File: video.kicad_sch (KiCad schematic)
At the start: 32 parts

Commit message: だいたい完成
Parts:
- removed U? (x2): 74LS195, symbol 74xx:74LS195
- removed U?: SST39SF010A, symbol RAM_ROM:SST39SF010A
- removed U?: TC551001, symbol RAM_ROM:TC551001
- added U10: TC551001, Package_DIP:DIP-32_W15.24mm, symbol RAM_ROM:TC551001
- added U11: SST39SF010A, Package_DIP:DIP-32_W15.24mm, symbol RAM_ROM:SST39SF010A
- added U8, U9: 74LS195, Package_DIP:DIP-16_W7.62mm, symbol 74xx:74LS195
- C17, C18: renamed from C?; footprint (none) -> Capacitor_THT:C_Disc_D3.0mm_W1.6mm_P2.50mm
- J1: renamed from J?; footprint (none) -> Connector_Dsub:DSUB-15-HD_Female_Horizontal_P2.29x1.98mm_EdgePinOffset3.03mm_Housed_MountingHolesOffset4.94mm
- JP1: renamed from JP?; footprint (none) -> Jumper:SolderJumper-3_P1.3mm_Bridged12_Pad1.0x1.5mm
- R1: renamed from R?; footprint (none) -> Resistor_THT:R_Axial_DIN0204_L3.6mm_D1.6mm_P5.08mm_Vertical
- R2, R3, R4, R5, R6, R7: renamed from R?; footprint (none) -> Resistor_SMD:R_0603_1608Metric_Pad0.98x0.95mm_HandSolder
- SW1: renamed from SW?; footprint (none) -> Button_Switch_THT:SW_DIP_SPSTx03_Slide_9.78x9.8mm_W7.62mm_P2.54mm
- U1, U2, U3: renamed from U?; footprint (none) -> Package_DIP:DIP-14_W7.62mm
- U4, U7: renamed from U?; footprint (none) -> Package_DIP:DIP-16_W7.62mm
- U5: renamed from U?; footprint (none) -> Package_DIP:DIP-20_W7.62mm
- U6: renamed from U?; footprint (none) -> Package_DIP:DIP-32_W15.24mm
- Y1: renamed from Y?; footprint (none) -> Crystal:Crystal_HC18-U_Vertical
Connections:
- net CLK: now also U2.9 (Q), U8.10 (CP), U9.10 (CP); no longer U2.5 (Q)
- net CRAM_Addr0: now also U10.12 (A0)
- net CRAM_Addr1: now also U10.11 (A1)
- net CRAM_Addr10: now also U10.5 (A7)
- net CRAM_Addr2: now also U10.10 (A2)
- net CRAM_Addr3: now also U10.23 (A10)
- net CRAM_Addr4: now also U10.9 (A3)
- net CRAM_Addr5: now also U10.8 (A4)
- net CRAM_Addr6: now also U10.7 (A5)
- net CRAM_Addr7: now also U10.26 (A9)
- net CRAM_Addr8: now also U10.6 (A6)
- net CRAM_Addr9: now also U10.27 (A8)
- net C_DATA0: now also U10.13 (Q0), U11.5 (A7)
- net C_DATA1: now also U10.14 (Q1), U11.6 (A6)
- net C_DATA2: now also U10.15 (Q2), U11.7 (A5)
- net C_DATA3: now also U10.21 (Q7), U11.8 (A4)
- net C_DATA4: now also U10.20 (Q6), U11.9 (A3)
- net C_DATA5: now also U10.19 (Q5), U11.10 (A2)
- net C_DATA6: now also U10.18 (Q4), U11.11 (A1)
- net C_DATA7: now also U10.17 (Q3), U11.12 (A0)
- net GND: now also U10.16 (GND), U10.2 (A16), U10.22 (~{CS1}), U10.28 (A13), U10.3 (A14), U10.31 (A15), U10.4 (A12), U11.16 (GND), U11.2 (A16), U11.22 (~{CE}), U11.24 (~{OE}), U11.25 (A11), U11.28 (A13), U11.29 (A14), U11.3 (A15), U11.4 (A12), U8.2 (J), U8.3 (~{K}), U8.8 (GND), U9.8 (GND)
- net H_COUNT_RS: now also U3.5; no longer U3.2
- net VCC: now also U1.5, U2.1 (~{R}), U2.10 (~{S}), U2.13 (~{R}), U2.4 (~{S}), U10.30 (CE2), U10.32 (VCC), U11.31 (~{WE}), U11.32 (VDD), U8.1 (~{MR}), U8.16 (VCC), U9.1 (~{MR}), U9.16 (VCC); no longer U2.1 (~{R}), U2.10 (~{S}), U2.13 (~{R}), U2.4 (~{S})
- net V_Addr1: now also U11.27 (A8)
- net V_Addr2: now also U11.26 (A9)
- net V_Addr3: now also U11.23 (A10)
- net Visible: now also U3.2; no longer U3.10
- net /CLK: now also U2.12 (D), U2.3 (C), U2.8 (~{Q}); no longer U2.11 (C), U2.2 (D), U2.6 (~{Q})
- net /PE: now also U2.2 (D), U3.8; no longer U2.12 (D), U3.11
- net ~{OE}: now also U10.24 (~{OE})
- net ~{WE}: now also U10.29 (RW)
- net at U1.4: now also U2.11 (C); no longer U2.3 (C)
- net at JP1.2 (C): now also U10.25 (A11)
- net at U3.9: now also U4.9 (Q0)
- net at U3.4, U4.6 (Q2): now also U3.12; no longer U3.1
- net at U3.3: now also SW1.1, SW1.2, SW1.3; no longer U4.11 (Reset)
- net at U3.13: now also U4.7 (Q1); no longer U3.6
- net at U1.10: no longer U1.5
- new net: U2.6 (~{Q}), U8.9 (~{PE}), U9.9 (~{PE})
- new net: U3.1, U9.12 (Q3)
- new net: U8.12 (Q3), U9.2 (J), U9.3 (~{K})
- new net: U3.10, U3.11
- new net: U3.6, U4.11 (Reset)
- new net CG_data0: U11.21 (Q7), U8.4 (P0)
- new net CG_data1: U11.20 (Q6), U8.5 (P1)
- new net CG_data2: U11.19 (Q5), U8.6 (P2)
- new net CG_data3: U11.18 (Q4), U8.7 (P3)
- new net CG_data4: U11.17 (Q3), U9.4 (P0)
- new net CG_data5: U11.15 (Q2), U9.5 (P1)
- new net CG_data6: U11.14 (Q1), U9.6 (P2)
- new net CG_data7: U11.13 (Q0), U9.7 (P3)
- no-connect marks 26 -> 28
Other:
- moved on the sheet: U1C, U1D, U2A, U3A, U3B, U3C, U3D

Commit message: 信号生成部設計完了
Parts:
- renumbered U9 to U10, U10 to U11, U11 to U12, U3 to U4, U4 to U5, U5 to U6, U6 to U7, U7 to U8, U8 to U9
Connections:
- net GND: now also U7.2 (A16)
- no-connect marks 28 -> 27

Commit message: 完成版
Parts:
- added RN1: R_Network04, Resistor_THT:R_Array_SIP5, symbol Device:R_Network04
- added SW2: SW_DIP_x04, Button_Switch_THT:SW_DIP_SPSTx04_Piano_10.8x11.72mm_W7.62mm_P2.54mm, symbol Switch:SW_DIP_x04
- added TP1, TP2, TP3: TestPoint, TestPoint:TestPoint_THTPad_D1.0mm_Drill0.5mm, symbol Connector:TestPoint
- JP1: footprint Jumper:SolderJumper-3_P1.3mm_Bridged12_Pad1.0x1.5mm -> Jumper:SolderJumper-3_P1.3mm_Open_RoundedPad1.0x1.5mm
- SW1: footprint Button_Switch_THT:SW_DIP_SPSTx03_Slide_9.78x9.8mm_W7.62mm_P2.54mm -> Button_Switch_THT:SW_DIP_SPSTx03_Piano_10.8x9.18mm_W7.62mm_P2.54mm
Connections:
- net GND: now also RN1.1 (common); no longer U11.28 (A13), U12.25 (A11), U12.28 (A13), U12.29 (A14), U12.4 (A12)
- net H_Sync: now also TP1.1
- net VCC: now also U11.28 (A13), SW2.1, SW2.2, SW2.3, SW2.4
- net V_Sync: now also TP2.1
- net Visible: now also TP3.1
- new net F_mode0: RN1.5 (R4), SW2.5, U12.25 (A11)
- new net F_mode1: RN1.4 (R3), SW2.6, U12.4 (A12)
- new net F_mode2: RN1.3 (R2), SW2.7, U12.28 (A13)
- new net F_mode3: RN1.2 (R1), SW2.8, U12.29 (A14)

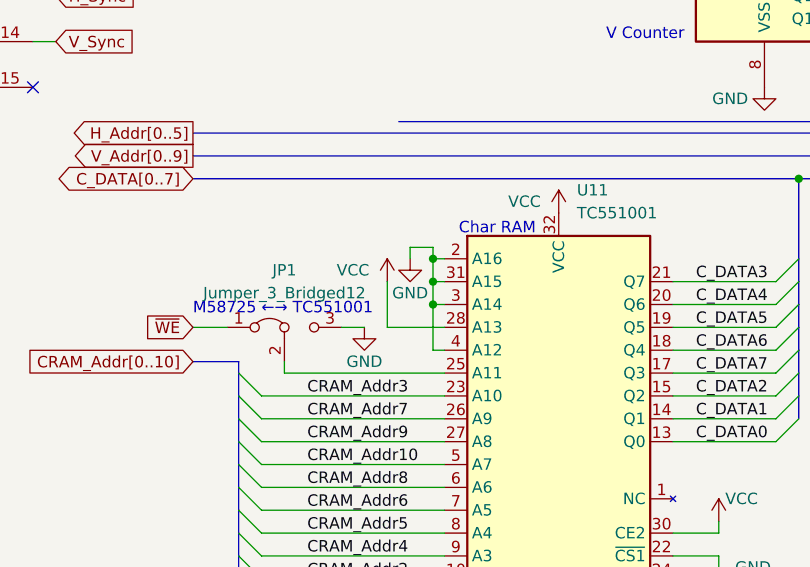
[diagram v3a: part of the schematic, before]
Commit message: 電源ライン増強他
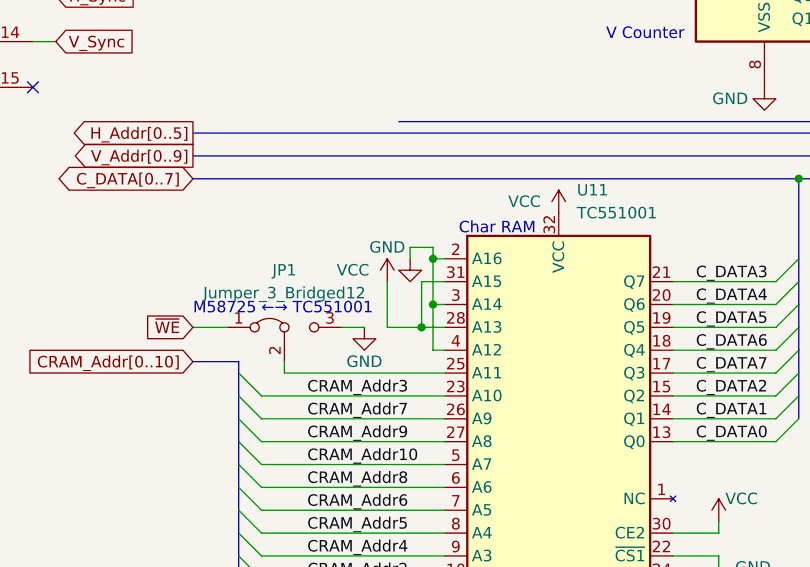
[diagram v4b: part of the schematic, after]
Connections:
- net GND: no longer U11.31 (A15)
- net VCC: now also U11.31 (A15)
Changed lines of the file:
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@@
   (junction (at 246.38 39.37) (diameter 0) (color 0 0 0 0)
   )
+  (junction (at 87.63 142.24) (diameter 0) (color 0 0 0 0)
+  )
   (junction (at 24.13 55.88) (diameter 0) (color 0 0 0 0)
-  )
-  (junction (at 88.9 137.16) (diameter 0) (color 0 0 0 0)
   )
   (junction (at 245.11 36.83) (diameter 0) (color 0 0 0 0)
@@
     (stroke (width 0) (type default) (color 0 0 0 0))
   )
+  (wire (pts (xy 90.17 137.16) (xy 87.63 137.16))
+    (stroke (width 0) (type default) (color 0 0 0 0))
+  )
   (wire (pts (xy 269.24 59.69) (xy 269.24 63.5))
     (stroke (width 0) (type default) (color 0 0 0 0))
@@
     (stroke (width 0) (type default) (color 0 0 0 0))
   )
-  (wire (pts (xy 83.82 142.24) (xy 90.17 142.24))
+  (wire (pts (xy 83.82 142.24) (xy 87.63 142.24))
     (stroke (width 0) (type default) (color 0 0 0 0))
   )
@@
     (stroke (width 0) (type default) (color 0 0 0 0))
   )
+  (wire (pts (xy 87.63 137.16) (xy 87.63 142.24))
+    (stroke (width 0) (type default) (color 0 0 0 0))
+  )
   (wire (pts (xy 207.01 57.15) (xy 209.55 57.15))
     (stroke (width 0) (type default) (color 0 0 0 0))
@@
     (stroke (width 0) (type default) (color 0 0 0 0))
   )
+  (wire (pts (xy 87.63 142.24) (xy 90.17 142.24))
+    (stroke (width 0) (type default) (color 0 0 0 0))
+  )
   (wire (pts (xy 72.39 147.32) (xy 90.17 147.32))
     (stroke (width 0) (type default) (color 0 0 0 0))
@@
     (stroke (width 0) (type default) (color 0 0 0 0))
   )
-  (wire (pts (xy 88.9 134.62) (xy 88.9 137.16))
+  (wire (pts (xy 88.9 134.62) (xy 88.9 139.7))
     (stroke (width 0) (type default) (color 0 0 0 0))
   )
@@
     (stroke (width 0) (type default) (color 0 0 0 0))
   )
-  (wire (pts (xy 88.9 137.16) (xy 88.9 139.7))
-    (stroke (width 0) (type default) (color 0 0 0 0))
-  )
   (wire (pts (xy 69.85 175.26) (xy 90.17 175.26))
     (stroke (width 0) (type default) (color 0 0 0 0))
@@
   )
   (wire (pts (xy 207.01 64.77) (xy 209.55 64.77))
-    (stroke (width 0) (type default) (color 0 0 0 0))
-  )
-  (wire (pts (xy 88.9 137.16) (xy 90.17 137.16))
     (stroke (width 0) (type default) (color 0 0 0 0))
   )
@@
       (effects (font (size 1.27 1.27)) hide)
     )
-    (property "Value" "GND" (id 1) (at 86.36 138.43 0))
+    (property "Value" "GND" (id 1) (at 83.82 133.35 0))
     (property "Footprint" "" (id 2) (at 86.36 134.62 0)
       (effects (font (size 1.27 1.27)) hide)

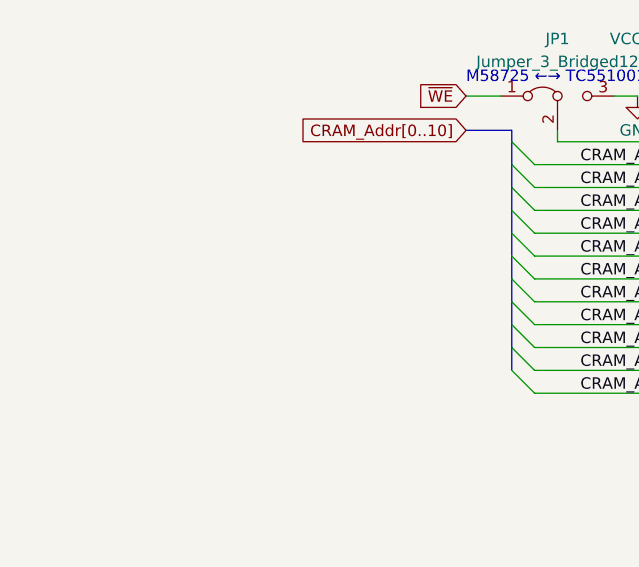
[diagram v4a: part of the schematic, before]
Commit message: 内部バスプルアップ追加他/基板製造バージョン
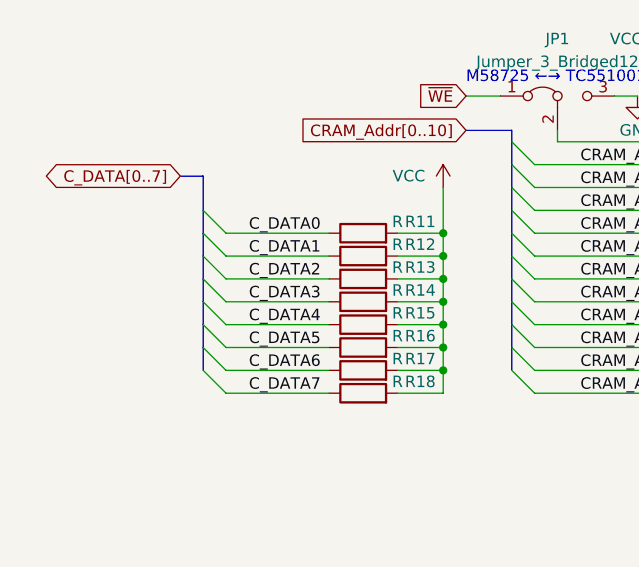
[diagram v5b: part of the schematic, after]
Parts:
- added R11, R12, R13, R14, R15, R16, R17, R18: R, Resistor_SMD:R_0603_1608Metric_Pad0.98x0.95mm_HandSolder, symbol Device:R
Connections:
- net C_DATA0: now also R11.1
- net C_DATA1: now also R12.1
- net C_DATA2: now also R13.1
- net C_DATA3: now also R14.1
- net C_DATA4: now also R15.1
- net C_DATA5: now also R16.1
- net C_DATA6: now also R17.1
- net C_DATA7: now also R18.1
- net VCC: now also R11.2, R12.2, R13.2, R14.2, R15.2, R16.2, R17.2, R18.2

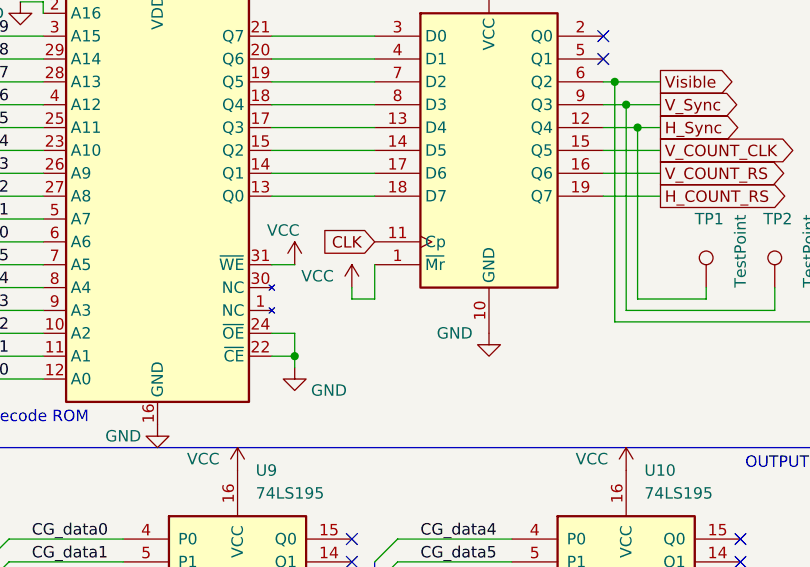
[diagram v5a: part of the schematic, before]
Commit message: VGAの入出力インターフェイス修正
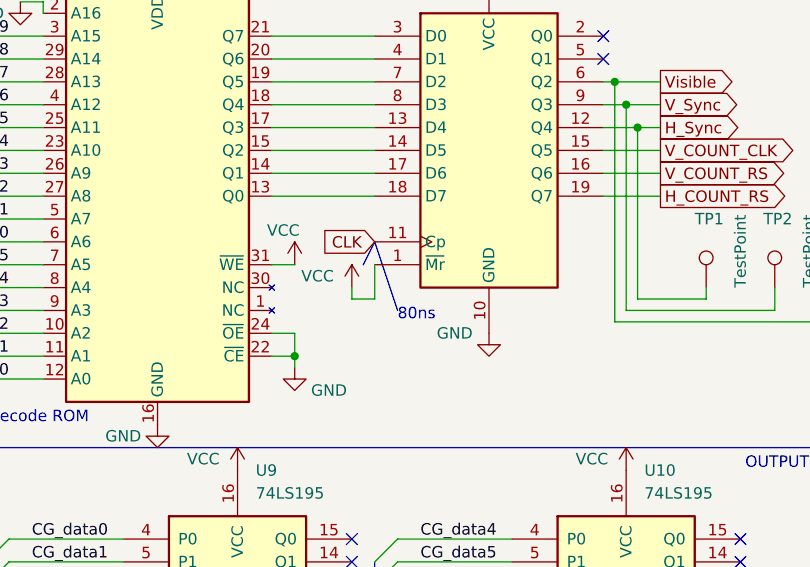
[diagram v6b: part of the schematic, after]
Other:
- note added: "80ns"
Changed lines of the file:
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@@
     (stroke (width 0) (type default) (color 0 0 0 0))
+  )
+  (polyline (pts (xy 218.44 54.61) (xy 220.98 62.23))
+    (stroke (width 0) (type solid) (color 0 0 0 0))
   )
   (wire (pts (xy 83.82 137.16) (xy 83.82 142.24))
@@
   (wire (pts (xy 54.61 170.18) (xy 59.69 170.18))
     (stroke (width 0) (type default) (color 0 0 0 0))
+  )
+  (polyline (pts (xy 217.17 57.15) (xy 218.44 54.61))
+    (stroke (width 0) (type solid) (color 0 0 0 0))
   )
   (wire (pts (xy 146.05 16.51) (xy 146.05 26.67))
@@
     (effects (font (size 1.27 1.27)) (justify right bottom))
   )
+  (text "80ns" (at 220.98 63.5 0)
+    (effects (font (size 1.27 1.27)) (justify left bottom))
+  )
   (text "OUTPUT" (at 266.7 80.01 180)

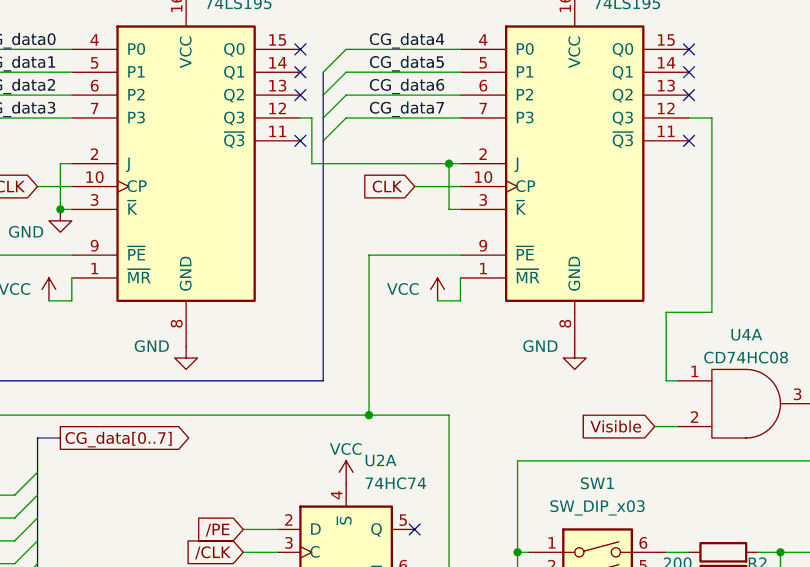
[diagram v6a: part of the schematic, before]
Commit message: VRAMアクセス中の出力イネーブルを追加
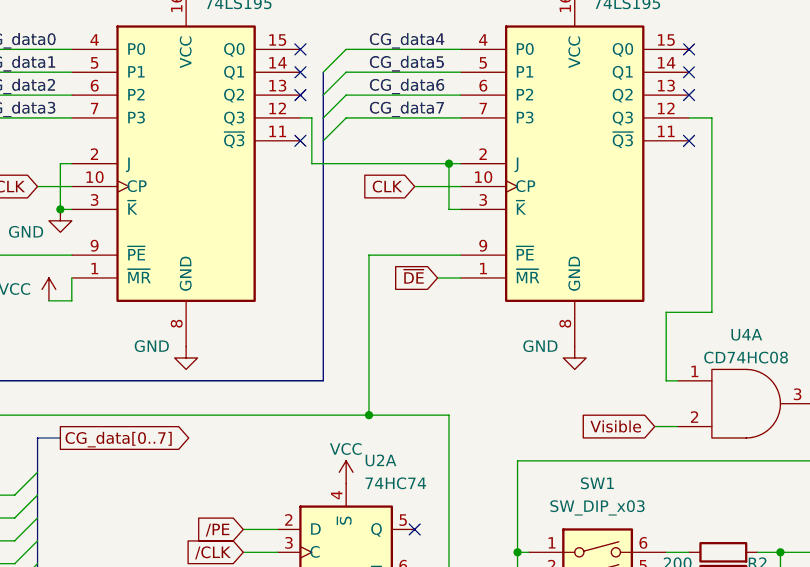
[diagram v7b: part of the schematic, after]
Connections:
- net VCC: no longer U10.1 (~{MR})
- new net ~{DE}: U10.1 (~{MR})
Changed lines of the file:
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@@
-    (stroke (width 0) (type default) (color 0 0 0 0))
-  )
-  (wire (pts (xy 231.14 115.57) (xy 233.68 115.57))
     (stroke (width 0) (type default) (color 0 0 0 0))
   )
@@
     (stroke (width 0) (type default) (color 0 0 0 0))
   )
-  (wire (pts (xy 233.68 115.57) (xy 233.68 113.03))
-    (stroke (width 0) (type default) (color 0 0 0 0))
-  )
   (wire (pts (xy 26.67 43.18) (xy 33.02 43.18))
     (stroke (width 0) (type default) (color 0 0 0 0))
@@
   )
   (wire (pts (xy 171.45 170.18) (xy 173.99 170.18))
+    (stroke (width 0) (type default) (color 0 0 0 0))
+  )
+  (wire (pts (xy 231.14 113.03) (xy 233.68 113.03))
     (stroke (width 0) (type default) (color 0 0 0 0))
   )
@@
     (effects (font (size 1.27 1.27)) (justify right))
     (property "Intersheet References" "${INTERSHEET_REFS}" (id 0) (at 107.0488 29.1306 0)
+      (effects (font (size 1.27 1.27)) (justify right) hide)
+    )
+  )
+  (global_label "~{DE}" (shape input) (at 231.14 113.03 180) (fields_autoplaced)
+    (effects (font (size 1.27 1.27)) (justify right))
+    (property "Intersheet References" "${INTERSHEET_REFS}" (id 0) (at 226.3079 112.9506 0)
       (effects (font (size 1.27 1.27)) (justify right) hide)
     )
@@
     (pin "7")
   )
-  (symbol (lib_id "power:VCC") (at 231.14 115.57 0) (unit 1)
-    (in_bom yes) (on_board yes)
-    (property "Reference" "#PWR031" (id 0) (at 231.14 119.38 0)
-      (effects (font (size 1.27 1.27)) hide)
-    )
-    (property "Value" "VCC" (id 1) (at 227.33 114.3 0))
-    (property "Footprint" "" (id 2) (at 231.14 115.57 0)
-      (effects (font (size 1.27 1.27)) hide)
-    )
-    (property "Datasheet" "" (id 3) (at 231.14 115.57 0)
-      (effects (font (size 1.27 1.27)) hide)
-    )
-    (pin "1")
-  )
   (symbol (lib_id "power:GND") (at 194.31 74.93 0) (unit 1)
